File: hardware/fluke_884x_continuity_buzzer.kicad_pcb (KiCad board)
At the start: 4 copper layers, 70.8 x 59.8 mm, 65 parts, among them J2 Conn_01x02, J203 16 pin DIP socket, J204 16 pin DIP socket, J3 USB_B_Micro, P203 16 pin DIP plug, P204 16 pin DIP plug, U1 AZ117EH-3.3, U2 W25Q128JVS, U3 RP2040, Y1 ABLS-12.000MHZ-B4-T

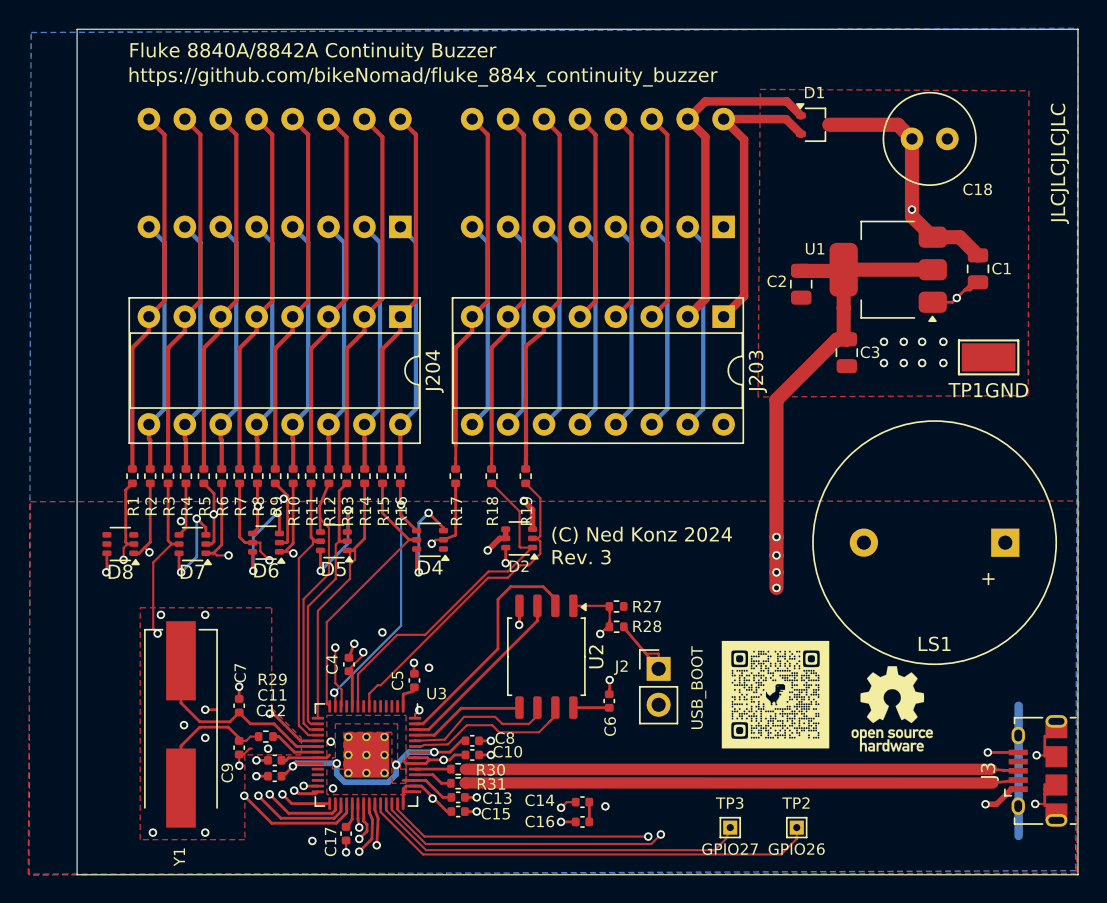
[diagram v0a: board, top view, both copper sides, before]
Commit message: Updated PCB layout to shorten board
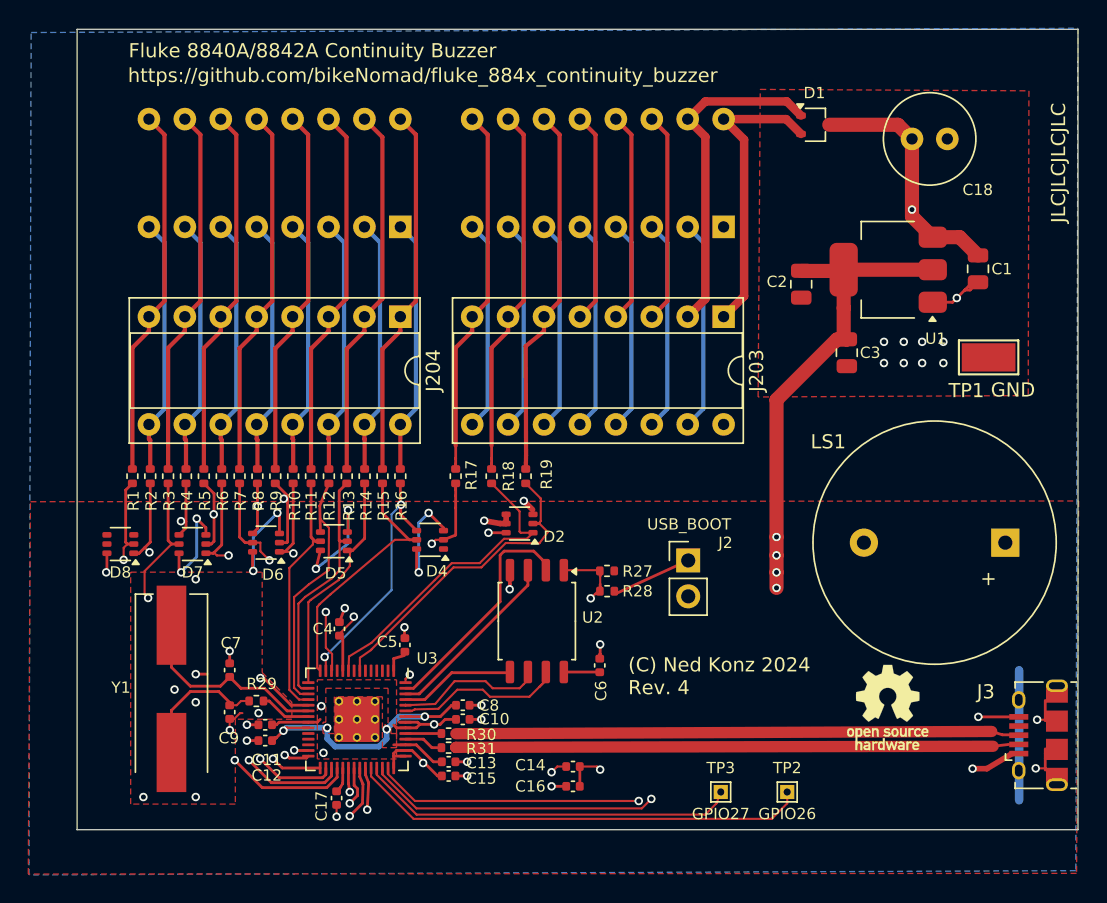
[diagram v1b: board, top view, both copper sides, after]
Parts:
- removed G***: LOGO, RP2040_minimal:qrcode
- moved J2 7.95 mm to (116.9, 63.0)
- moved C16 2.61 mm to (108.7, 78.9)
- moved R29 2.61 mm to (86.3, 72.9)
- moved C10 2.61 mm to (100.9, 74.2)
- moved C11 2.61 mm to (87.0, 74.6)
- moved C12 2.61 mm to (87.0, 75.7)
- moved C13 2.61 mm to (99.9, 77.2)
- moved C15 2.61 mm to (99.9, 78.2)
- moved C5 2.61 mm to (96.8, 68.9)
- moved C6 2.61 mm to (110.6, 70.4)
- moved C7 2.61 mm to (84.5, 70.7)
- moved C8 2.61 mm to (100.9, 73.2)
- moved C9 2.61 mm to (84.5, 73.7)
- moved R28 2.61 mm to (111.1, 65.1)
- moved R30 2.61 mm to (99.9, 75.2)
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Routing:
- net /GPIO29_ADC3: track 52.6 -> 43.8 mm
- net +3V3: track 104.7 -> 98.8 mm, vias 22 -> 20
- net G3_3V: track 19.6 -> 16.0 mm
- net PE_3V: track 35.7 -> 32.6 mm
- net G1_3V: track 33.4 -> 30.4 mm
- net PA_3V: track 30.1 -> 27.1 mm
- net G0_3V: track 33.0 -> 30.3 mm
- net PF_3V: track 33.5 -> 30.7 mm, vias 3 -> 2
- net PB_3V: track 33.8 -> 31.0 mm
- net PC_3V: track 26.3 -> 23.7 mm
- net PG_3V: track 28.8 -> 26.2 mm
- net PS3_3V: track 34.5 -> 32.2 mm
- net G2_3V: track 20.8 -> 18.6 mm
- net PD_3V: track 19.8 -> 17.6 mm
- net G4_3V: track 20.2 -> 18.2 mm
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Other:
- board size 70.8 x 59.8 mm -> 70.8 x 56.6 mm

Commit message: Exclude plugs and USB BOOT header from production
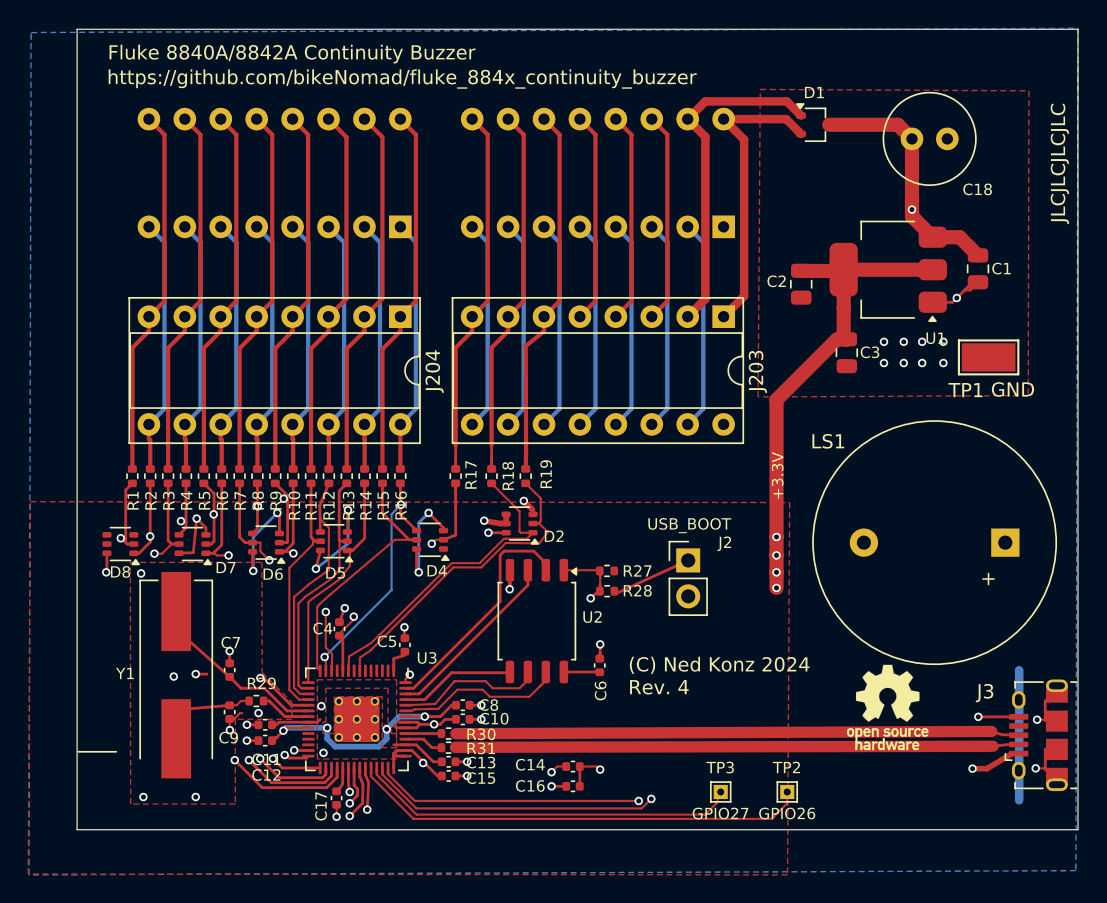
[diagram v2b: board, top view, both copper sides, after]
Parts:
- moved Y1 1.03 mm to (80.7, 71.1)
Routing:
- net Net-(C9-Pad1): track 9.51 -> 5.63 mm
- net /XIN: track 14.5 -> 12.1 mm
- net +3V3: track 98.8 -> 96.6 mm, vias 20 -> 19
- net PS2_3V: track 33.7 -> 34.9 mm
- net PB_3V: track 31.0 -> 31.8 mm
- net GND: vias 35 -> 34
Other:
- board text added: "+3.3V"

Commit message: Change to using external GND connection
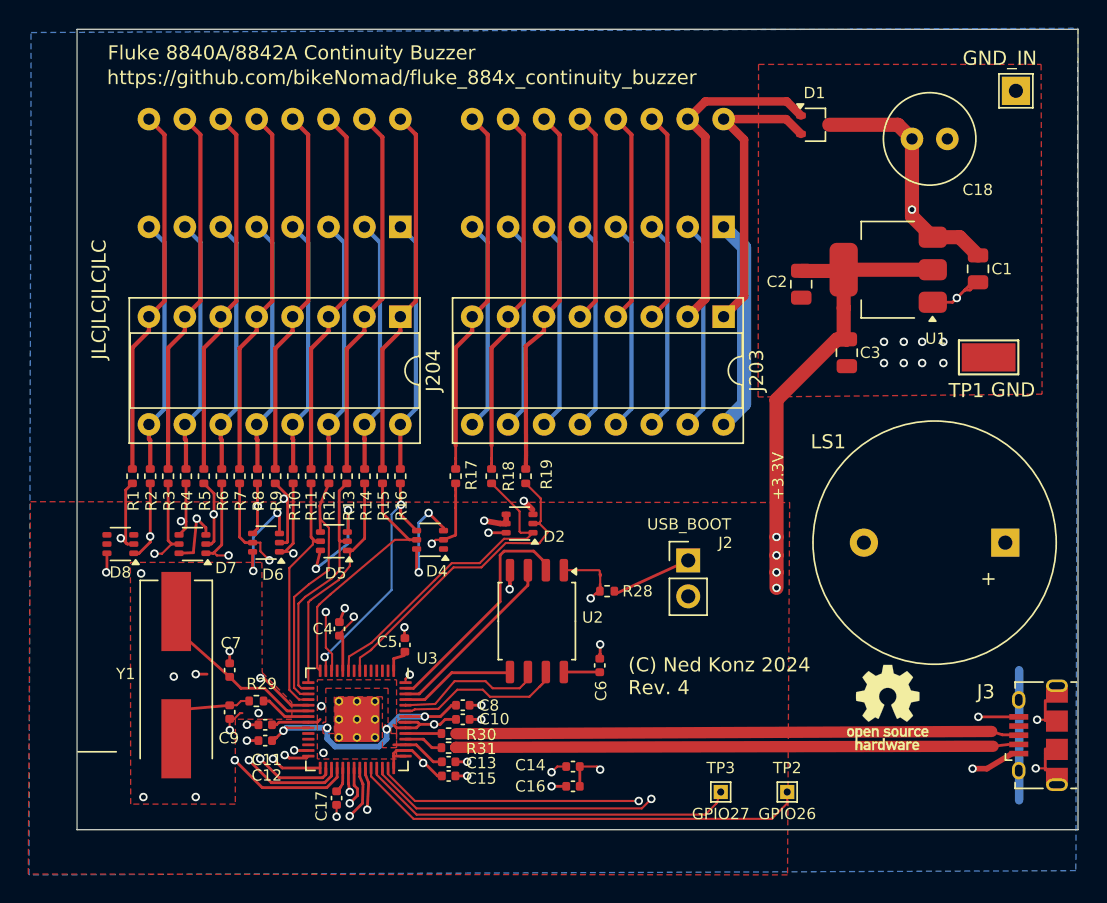
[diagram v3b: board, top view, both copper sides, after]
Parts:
- removed R27: DNF, Resistor_SMD:R_0402_1005Metric
- added TP4: GND_IN, TestPoint:TestPoint_THTPad_2.0x2.0mm_Drill1.0mm, F.Cu at (140.1, 29.8)
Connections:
- J203 pad 16: GND -> /GND2
- P203 pad 1: GND -> /GND2
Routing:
- net GND: track 57.3 -> 42.1 mm
- net /GND2: track 0.00 -> 15.2 mm
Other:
- board text added: "GND_IN"
